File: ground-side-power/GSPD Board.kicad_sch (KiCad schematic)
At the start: 0 parts

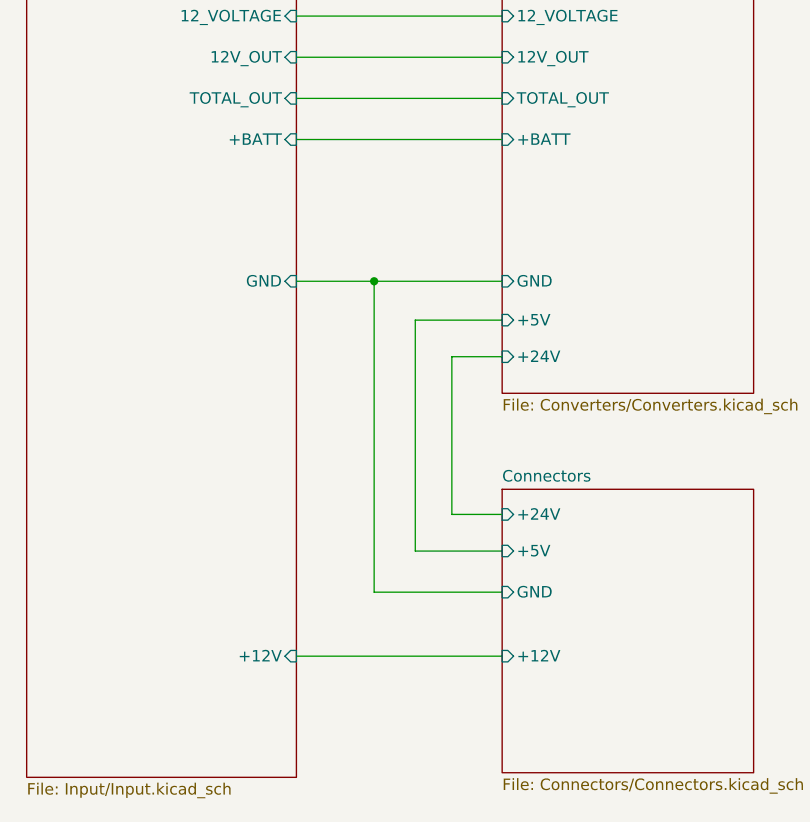
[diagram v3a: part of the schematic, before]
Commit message: Created layout for the footprints for each board
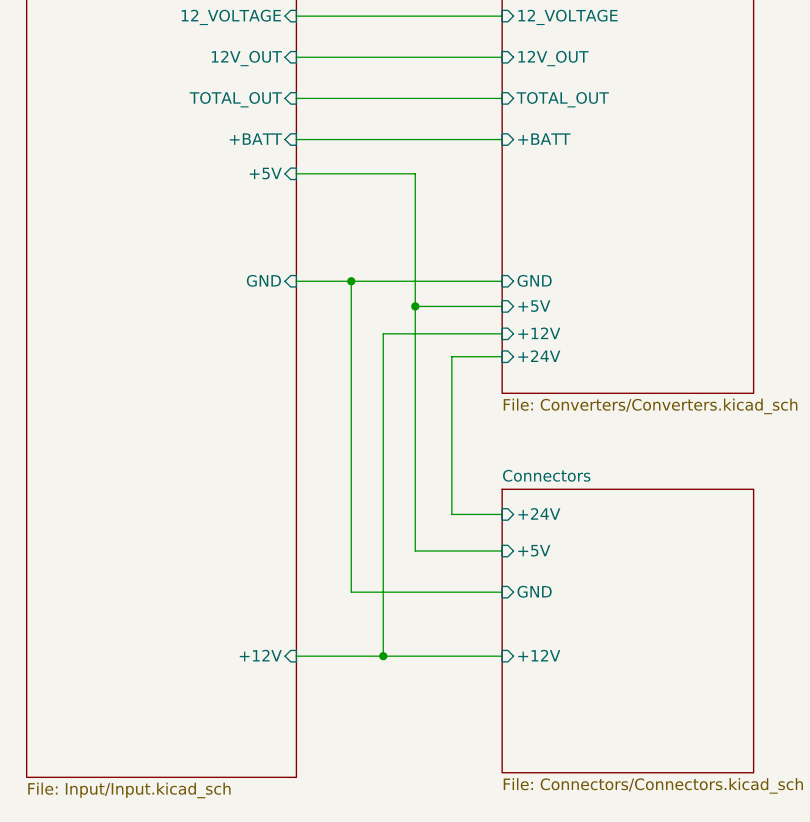
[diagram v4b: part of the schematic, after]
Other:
- sheet Converters ports: added +12V; removed none
- sheet Input ports: added +5V; removed none
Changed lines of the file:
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@@
 (kicad_sch (version 20211123) (generator eeschema)
   (paper "A4")
-  (junction (at 143.002 84.328) (diameter 0) (color 0 0 0 0)
+  (junction (at 144.018 125.984) (diameter 0) (color 0 0 0 0)
+  )
+  (junction (at 147.574 87.122) (diameter 0) (color 0 0 0 0)
+  )
+  (junction (at 140.462 84.328) (diameter 0) (color 0 0 0 0)
   )
   (polyline (pts (xy 13.208 197.104) (xy 13.208 157.734))
@@
     (stroke (width 0) (type default) (color 0 0 0 0))
   )
-  (wire (pts (xy 147.574 88.646) (xy 147.574 114.3))
-    (stroke (width 0) (type default) (color 0 0 0 0))
-  )
   (wire (pts (xy 157.226 110.236) (xy 151.638 110.236))
+    (stroke (width 0) (type default) (color 0 0 0 0))
+  )
+  (wire (pts (xy 144.018 125.984) (xy 157.226 125.984))
     (stroke (width 0) (type default) (color 0 0 0 0))
   )
@@
     (stroke (width 0) (type default) (color 0 0 0 0))
   )
+  (wire (pts (xy 144.018 90.17) (xy 157.226 90.17))
+    (stroke (width 0) (type default) (color 0 0 0 0))
+  )
   (polyline (pts (xy 13.208 157.734) (xy 65.913 157.734))
     (stroke (width 0) (type default) (color 0 0 0 0))
   )
-  (wire (pts (xy 143.002 118.872) (xy 157.226 118.872))
-    (stroke (width 0) (type default) (color 0 0 0 0))
-  )
-  (wire (pts (xy 147.574 88.646) (xy 157.226 88.646))
+  (wire (pts (xy 144.018 125.984) (xy 144.018 90.17))
+    (stroke (width 0) (type default) (color 0 0 0 0))
+  )
+  (wire (pts (xy 140.462 118.872) (xy 157.226 118.872))
+    (stroke (width 0) (type default) (color 0 0 0 0))
+  )
+  (wire (pts (xy 134.366 72.39) (xy 147.574 72.39))
+    (stroke (width 0) (type default) (color 0 0 0 0))
+  )
+  (wire (pts (xy 147.574 87.122) (xy 157.226 87.122))
     (stroke (width 0) (type default) (color 0 0 0 0))
   )
@@
     (stroke (width 0) (type solid) (color 0 0 0 0))
   )
-  (wire (pts (xy 143.002 84.328) (xy 143.002 118.872))
+  (wire (pts (xy 147.574 87.122) (xy 147.574 114.3))
+    (stroke (width 0) (type default) (color 0 0 0 0))
+  )
+  (wire (pts (xy 140.462 84.328) (xy 140.462 118.872))
     (stroke (width 0) (type default) (color 0 0 0 0))
   )
@@
     (stroke (width 0) (type default) (color 0 0 0 0))
   )
-  (wire (pts (xy 134.366 125.984) (xy 157.226 125.984))
-    (stroke (width 0) (type default) (color 0 0 0 0))
-  )
-  (wire (pts (xy 143.002 84.328) (xy 157.226 84.328))
+  (wire (pts (xy 134.366 125.984) (xy 144.018 125.984))
     (stroke (width 0) (type default) (color 0 0 0 0))
   )
@@
     (stroke (width 0) (type solid) (color 0 0 0 0))
   )
-  (wire (pts (xy 134.366 84.328) (xy 143.002 84.328))
+  (wire (pts (xy 140.462 84.328) (xy 157.226 84.328))
+    (stroke (width 0) (type default) (color 0 0 0 0))
+  )
+  (wire (pts (xy 147.574 72.39) (xy 147.574 87.122))
+    (stroke (width 0) (type default) (color 0 0 0 0))
+  )
+  (wire (pts (xy 134.366 84.328) (xy 140.462 84.328))
     (stroke (width 0) (type default) (color 0 0 0 0))
   )
@@
       (effects (font (size 1.27 1.27)) (justify left))
     )
-    (pin "+5V" input (at 157.226 88.646 180)
+    (pin "+5V" input (at 157.226 87.122 180)
       (effects (font (size 1.27 1.27)) (justify left))
     )
@@
     )
     (pin "+BATT" input (at 157.226 68.58 180)
+      (effects (font (size 1.27 1.27)) (justify left))
+    )
+    (pin "+12V" input (at 157.226 90.17 180)
       (effects (font (size 1.27 1.27)) (justify left))
     )
@@
       (effects (font (size 1.27 1.27)) (justify right))
     )
+    (pin "+5V" input (at 134.366 72.39 0)
+      (effects (font (size 1.27 1.27)) (justify right))
+    )
   )
   (sheet_instances
@@
       (reference "#PWR0102") (unit 1) (value "+24V") (footprint "")
     )
+    (path "/c08ef0af-6eeb-4957-ab7b-ce5d90f9f501/32ee28c2-a56b-4d24-830e-1cd0f88a3351"
+      (reference "#PWR0103") (unit 1) (value "+5V") (footprint "")
+    )
     (path "/c08ef0af-6eeb-4957-ab7b-ce5d90f9f501/0e1f6de9-01e2-4aa1-b10b-87b597b05612"
       (reference "C1") (unit 1) (value "100uF") (footprint "Capacitor_SMD:C_1206_3216Metric_Pad1.33x1.80mm_HandSolder")
@@
       (reference "J9") (unit 1) (value "Conn_01x03_Female") (footprint "GSP:TB005-762-03BE")
     )
-    (path "/1ed0032b-87a3-463e-b758-0066bb0761d6/2e272802-f871-4974-a8fa-3c4727a84407"
-      (reference "J10") (unit 1) (value "Conn_01x02_Female") (footprint "GSP:OSTTA020161")
+    (path "/1ed0032b-87a3-463e-b758-0066bb0761d6/98d6fa8d-7f4a-4e31-88c5-c8c41ad7826a"
+      (reference "J10") (unit 1) (value "Conn_01x03_Female") (footprint "GSP:TB005-762-03BE")
     )
     (path "/1ed0032b-87a3-463e-b758-0066bb0761d6/81f8443e-3717-485b-96f3-864e2dcd1ef4"
       (reference "J11") (unit 1) (value "Conn_01x03_Female") (footprint "GSP:TB005-762-03BE")
     )
-    (path "/1ed0032b-87a3-463e-b758-0066bb0761d6/510154d0-6e6b-43d4-bb63-af9283b3ce65"
-      (reference "J12") (unit 1) (value "Conn_01x03_Female") (footprint "GSP:TB005-762-03BE")
+    (path "/1ed0032b-87a3-463e-b758-0066bb0761d6/e7c756b3-86d0-437a-ae8e-182bdb94fe68"
+      (reference "J12") (unit 1) (value "Conn_01x04_Female") (footprint "GSP:EB21A-04-D")
     )
     (path "/1ed0032b-87a3-463e-b758-0066bb0761d6/1afe7a7c-798a-4960-aef3-7003f2220361"
@@
       (reference "J25") (unit 1) (value "Extra M12") (footprint "GSP:EB21A-04-D")
     )
+    (path "/c08ef0af-6eeb-4957-ab7b-ce5d90f9f501/6539d8dc-ec91-4bfc-8c20-4989b12a36ad"
+      (reference "J26") (unit 1) (value "Conn_01x02_Female") (footprint "GSP:OSTTA020161")
+    )
+    (path "/1ed0032b-87a3-463e-b758-0066bb0761d6/9d8f755f-f8c3-4e58-a584-f1f1f662fd19"
+      (reference "J27") (unit 1) (value "Conn_01x02_Female") (footprint "GSP:OSTTA020161")
+    )
     (path "/c08ef0af-6eeb-4957-ab7b-ce5d90f9f501/37cbc6aa-142d-4246-bbd1-db946c775626"

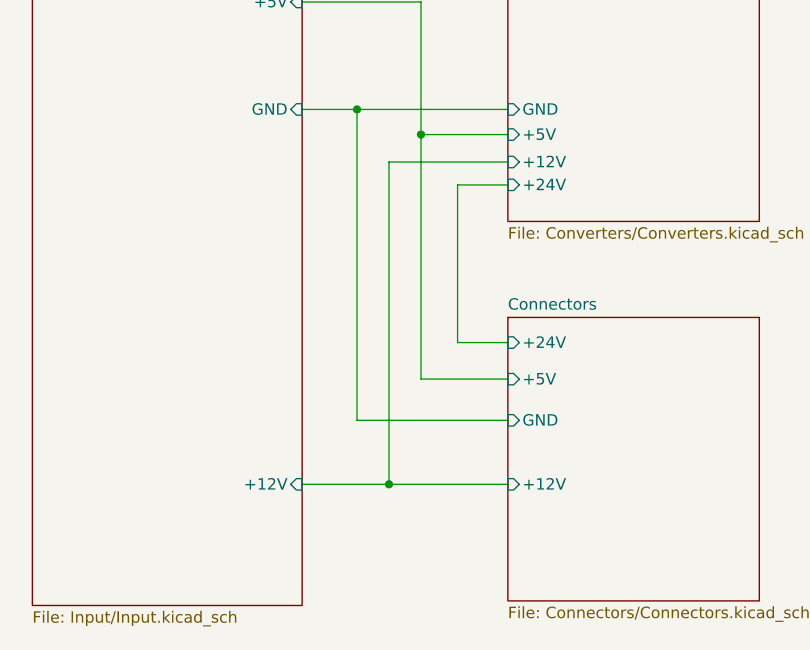
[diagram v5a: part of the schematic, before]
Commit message: Address Input and Converter Comments
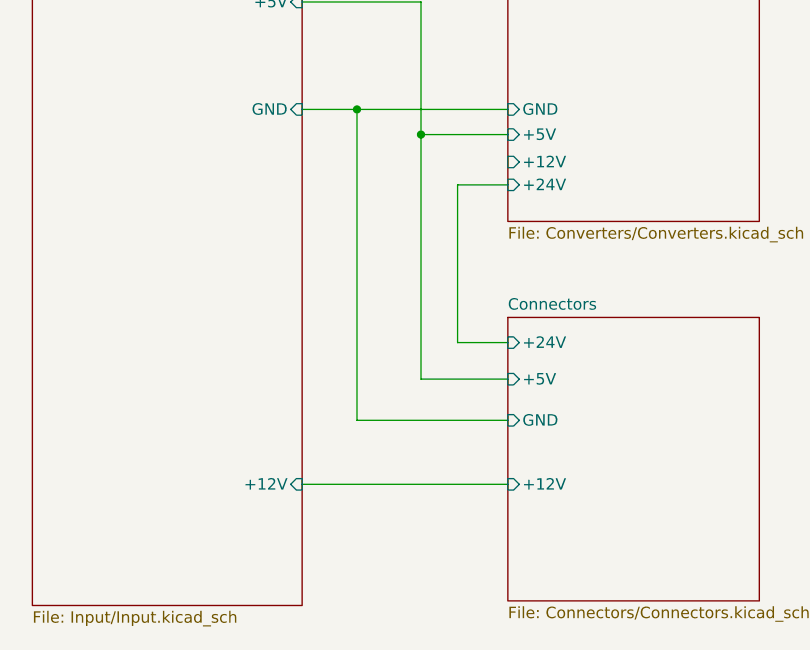
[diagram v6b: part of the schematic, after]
